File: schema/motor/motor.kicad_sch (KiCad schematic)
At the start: 13 parts, among them IC1 RP2040_ZERO, J1 Conn_01x06, J2 Conn_02x04_Odd_Even, J4 Conn_01x04_Pin

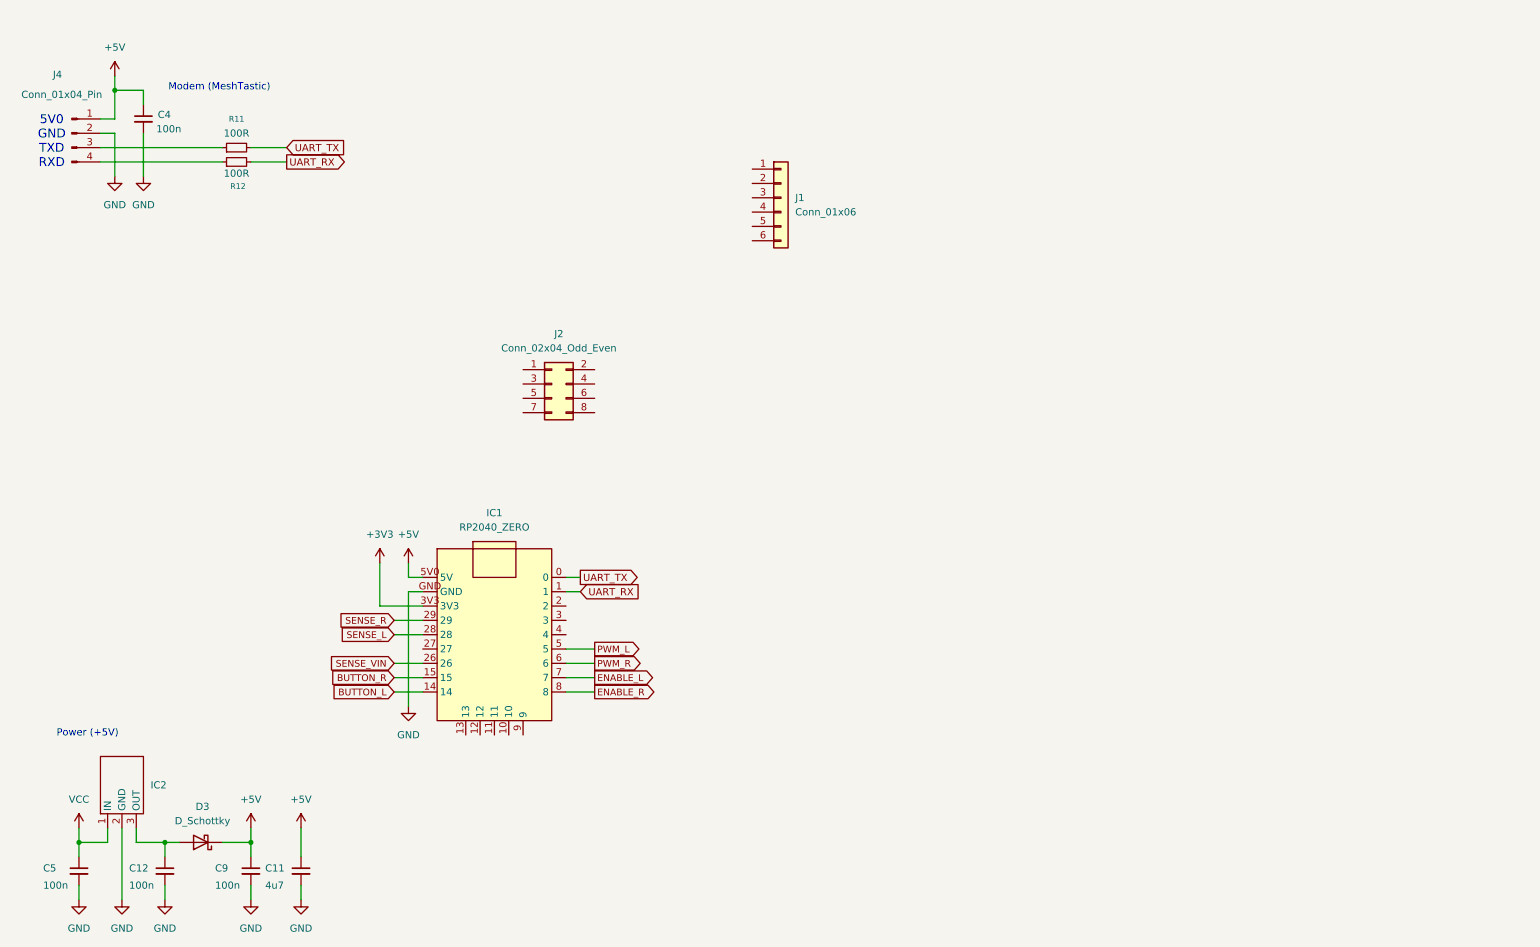
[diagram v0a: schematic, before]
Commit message: building motor pcb
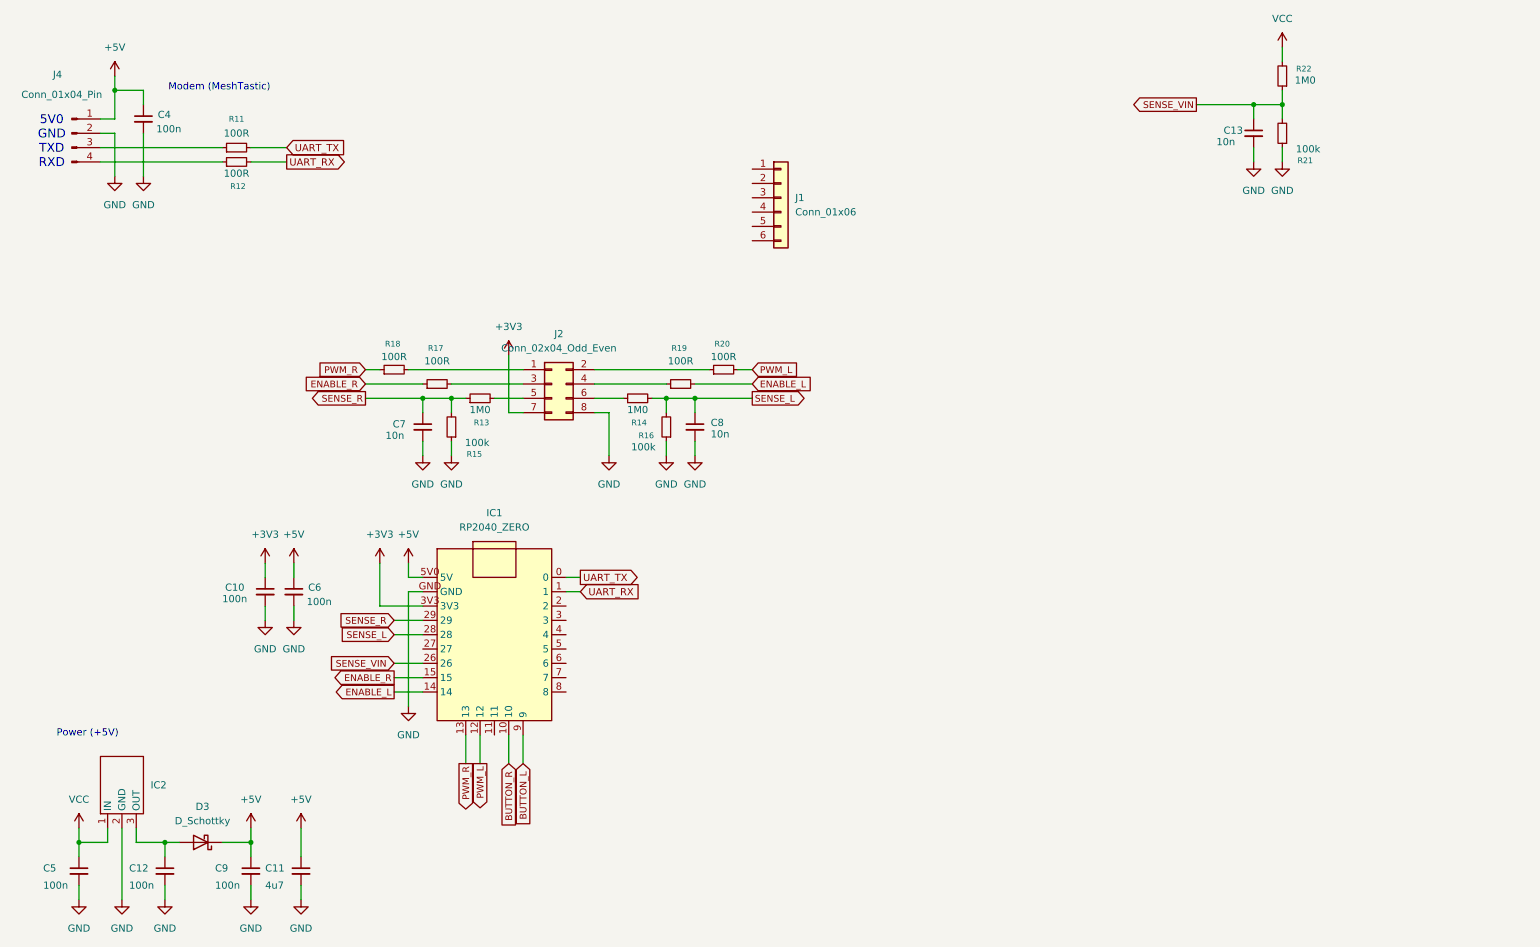
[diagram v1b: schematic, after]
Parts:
- added C10, C6: 100n, Capacitor_SMD:C_0603_1608Metric, symbol Device:C_Small
- added C13, C7, C8: 10n, Capacitor_SMD:C_0603_1608Metric, symbol Device:C_Small
- added R13, R14, R22: 1M0, Resistor_SMD:R_0603_1608Metric, symbol Device:R_Small
- added R15, R16, R21: 100k, Resistor_SMD:R_0603_1608Metric, symbol Device:R_Small
- added R17, R18, R19, R20: 100R, Resistor_SMD:R_0603_1608Metric, symbol Device:R_Small
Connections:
- net +3V3: now also J2.7 (Pin_7), C10.1
- net +5V: now also C6.1
- net BUTTON_L: now also IC1.9; no longer IC1.14
- net BUTTON_R: now also IC1.10; no longer IC1.15
- net ENABLE_L: now also IC1.14, R19.2; no longer IC1.7
- net ENABLE_R: now also IC1.15, R17.1; no longer IC1.8
- net GND: now also J2.8 (Pin_8), C10.2, C13.2, C6.2, C7.2, C8.2, R15.1, R16.1, R21.1
- net PWM_L: now also IC1.12, R20.2; no longer IC1.5
- net PWM_R: now also IC1.13, R18.1; no longer IC1.6
- net SENSE_L: now also C8.1, R14.2, R16.2
- net SENSE_R: now also C7.1, R13.1, R15.2
- net SENSE_VIN: now also C13.1, R21.2, R22.1
- net VCC: now also R22.2
- net at J2.1 (Pin_1): now also R18.2
- net at J2.2 (Pin_2): now also R20.1
- net at J2.3 (Pin_3): now also R17.2
- net at J2.4 (Pin_4): now also R19.1
- net at J2.5 (Pin_5): now also R13.2
- net at J2.6 (Pin_6): now also R14.1

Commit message: motor driver layout nearly done
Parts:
- added D2, D4, D5: BAV99, Package_TO_SOT_SMD:SOT-23, symbol Diode:BAV99
- added H1, H2, H3, H4: MountingHole, MountingHole:MountingHole_3.2mm_M3, symbol Mechanical:MountingHole
- added Q1: DMG4800LK3-13, Package_TO_SOT_SMD:TO-252-3_TabPin2, symbol Device:Q_NMOS_GDS
- added R10, R23, R9: 1k0, Resistor_SMD:R_0603_1608Metric, symbol Device:R_Small
- added R2: 10k, Resistor_SMD:R_0603_1608Metric, symbol Device:R_Small
- added R3, R4, R5, R6: 100R, Resistor_SMD:R_0603_1608Metric, symbol Device:R_Small
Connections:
- net BUTTON_L: now also D4.3 (K), R5.1
- net BUTTON_R: now also D5.3 (K), R6.1
- net GND: now also J1.5 (Pin_5), D2.1 (K), D4.1 (K), D5.1 (K), Q1.3 (S), R2.2
- net VCC: now also J1.6 (Pin_6)
- net at J1.1 (Pin_1): now also R23.2, R6.2
- net at J1.2 (Pin_2): now also R10.2, R5.2
- net at J1.3 (Pin_3): now also R4.2, R9.2
- net at J1.4 (Pin_4): now also Q1.2 (D)
- net BUTTON: now reaches IC1.11
- net BUTTON: now also D2.3 (K), R4.1
- net LIGHT_ON: now reaches IC1.8
- net LIGHT_ON: now also R3.1
- new net: Q1.1 (G), R2.1, R3.2
- new net +3.3V: D2.2 (A), D4.2 (A), D5.2 (A), R10.1, R23.1, R9.1
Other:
- moved on the sheet: C13, C7, C8, J1, J2, R13, R14, R15, R16, R17, R18, R19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

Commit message: pravdepodobne starsi verze
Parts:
- removed D2, D4, D5: BAV99, Package_TO_SOT_SMD:SOT-23, symbol Diode:BAV99
- removed H1, H2, H3, H4: MountingHole, MountingHole:MountingHole_3.2mm_M3, symbol Mechanical:MountingHole
- removed R10, R23, R9: 1k0, Resistor_SMD:R_0603_1608Metric, symbol Device:R_Small
- removed R4, R5, R6: 100R, Resistor_SMD:R_0603_1608Metric, symbol Device:R_Small
- added R8: 4k7, Resistor_SMD:R_0603_1608Metric, symbol Device:R_Small
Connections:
- net +3V3: now also R8.1
- net BUTTON: now also IC1.8, R8.2; no longer IC1.11
- net LIGHT_ON: now also IC1.11; no longer IC1.8
- net at J1.1 (Pin_1): now also Q1.2 (D)
- net at J1.4 (Pin_4): no longer Q1.2 (D)
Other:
- moved on the sheet: C13, Q1, R2, R21, R22, R3

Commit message: layout done, silk screen needed
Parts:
- added C14: 100n, Capacitor_SMD:C_0603_1608Metric, symbol Device:C_Small
- added D1, D2, D4: BAV99, Package_TO_SOT_SMD:SOT-23, symbol Diode:BAV99
- added H1, H2, H3, H4: MountingHole, MountingHole:MountingHole_3.2mm_M3, symbol Mechanical:MountingHole
- added R10, R9: 1k0, Resistor_SMD:R_0603_1608Metric, symbol Device:R_Small
- added R23, R24, R25: 100R, Resistor_SMD:R_0603_1608Metric, symbol Device:R_Small
- J4: now left out of the parts list
- R8: value 4k7 -> 1k0
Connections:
- net +3V3: now also C14.1, D1.2 (A), D2.2 (A), D4.2 (A), R10.1, R9.1
- net BUTTON: now also IC1.11, R23.1; no longer IC1.8, R8.2
- net BUTTON_L: now also R24.1
- net BUTTON_R: now also R25.1
- net GND: now also C14.2, D1.1 (K), D2.1 (K), D4.1 (K)
- net LIGHT_ON: now also IC1.8; no longer IC1.11
- net at J1.1 (Pin_1): now also D1.3 (K), R10.2, R25.2; no longer Q1.2 (D)
- net at J1.2 (Pin_2): now also D2.3 (K), R24.2, R9.2
- net at J1.3 (Pin_3): now also R8.2, D4.3 (K), R23.2
- net at J1.4 (Pin_4): now also Q1.2 (D)
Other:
- moved on the sheet: C13, Q1, R2, R21, R22, R3, R8

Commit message: chicken squasher hw v1.0 - final touch, fabrication
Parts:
- IC2: value (none) -> +5V REG
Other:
- note added: "Chicken Squasher v0.1"
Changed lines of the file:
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@@
 		)
 	)
+	(text "Chicken Squasher v0.1"
+		(exclude_from_sim no)
+		(at 230.124 175.26 0)
+		(effects
+			(font
+				(size 3.81 3.81)
+			)
+		)
+	)
 	(text "Modem (MeshTastic)"
 		(exclude_from_sim no)
@@
 		(fields_autoplaced yes)
 		(property "Reference" "IC2"
-			(at 44.45 156.2099 0)
+			(at 44.45 154.9399 0)
 			(show_name no)
 			(do_not_autoplace no)
@@
 			)
 		)
-		(property "Value" ""
+		(property "Value" "+5V REG"
 			(at 44.45 157.4799 0)
 			(show_name no)
